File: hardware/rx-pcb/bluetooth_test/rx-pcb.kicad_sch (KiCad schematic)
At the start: 32 parts, among them J1 Conn_01x05_Pin, J2 Conn_01x04_Pin, J4 Conn_01x04_Pin, SW1 SW_SPST, U1 STM32WB05KZV6TR, U2 STS4L-AD1B-R3, U3 LMT70AYFQR, X1 Q22FA12800025, X2 ABS07-32.768KHZ-1-T

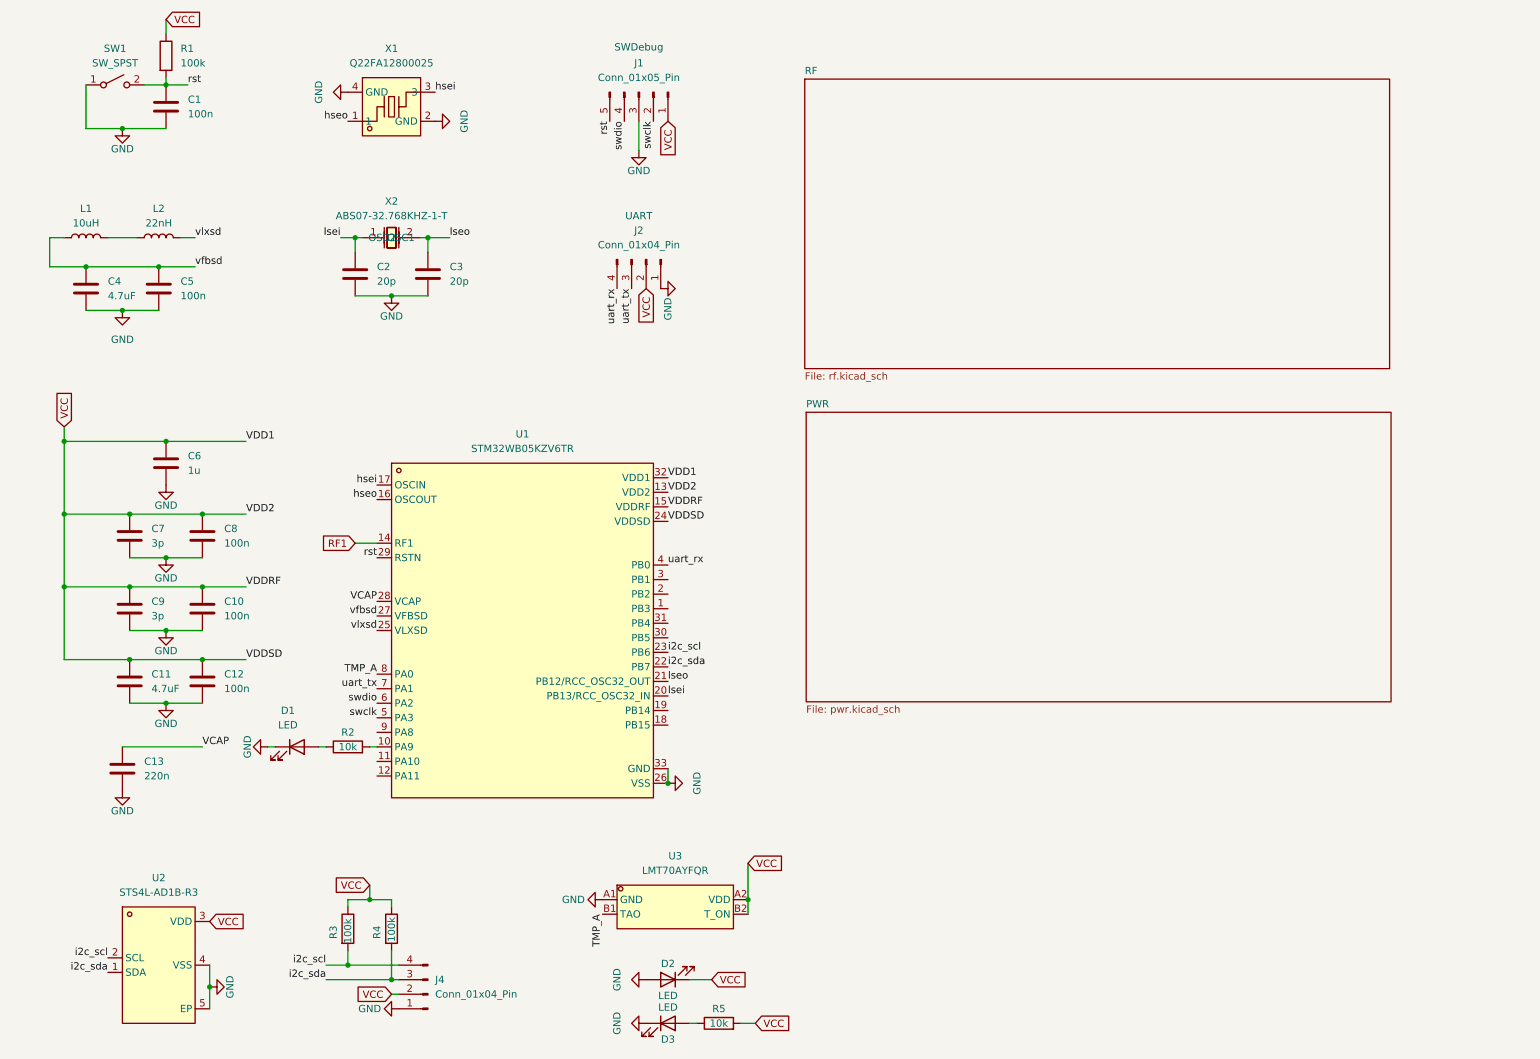
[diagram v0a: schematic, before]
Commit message: added selected diodes and bank capacitor. began board layout.
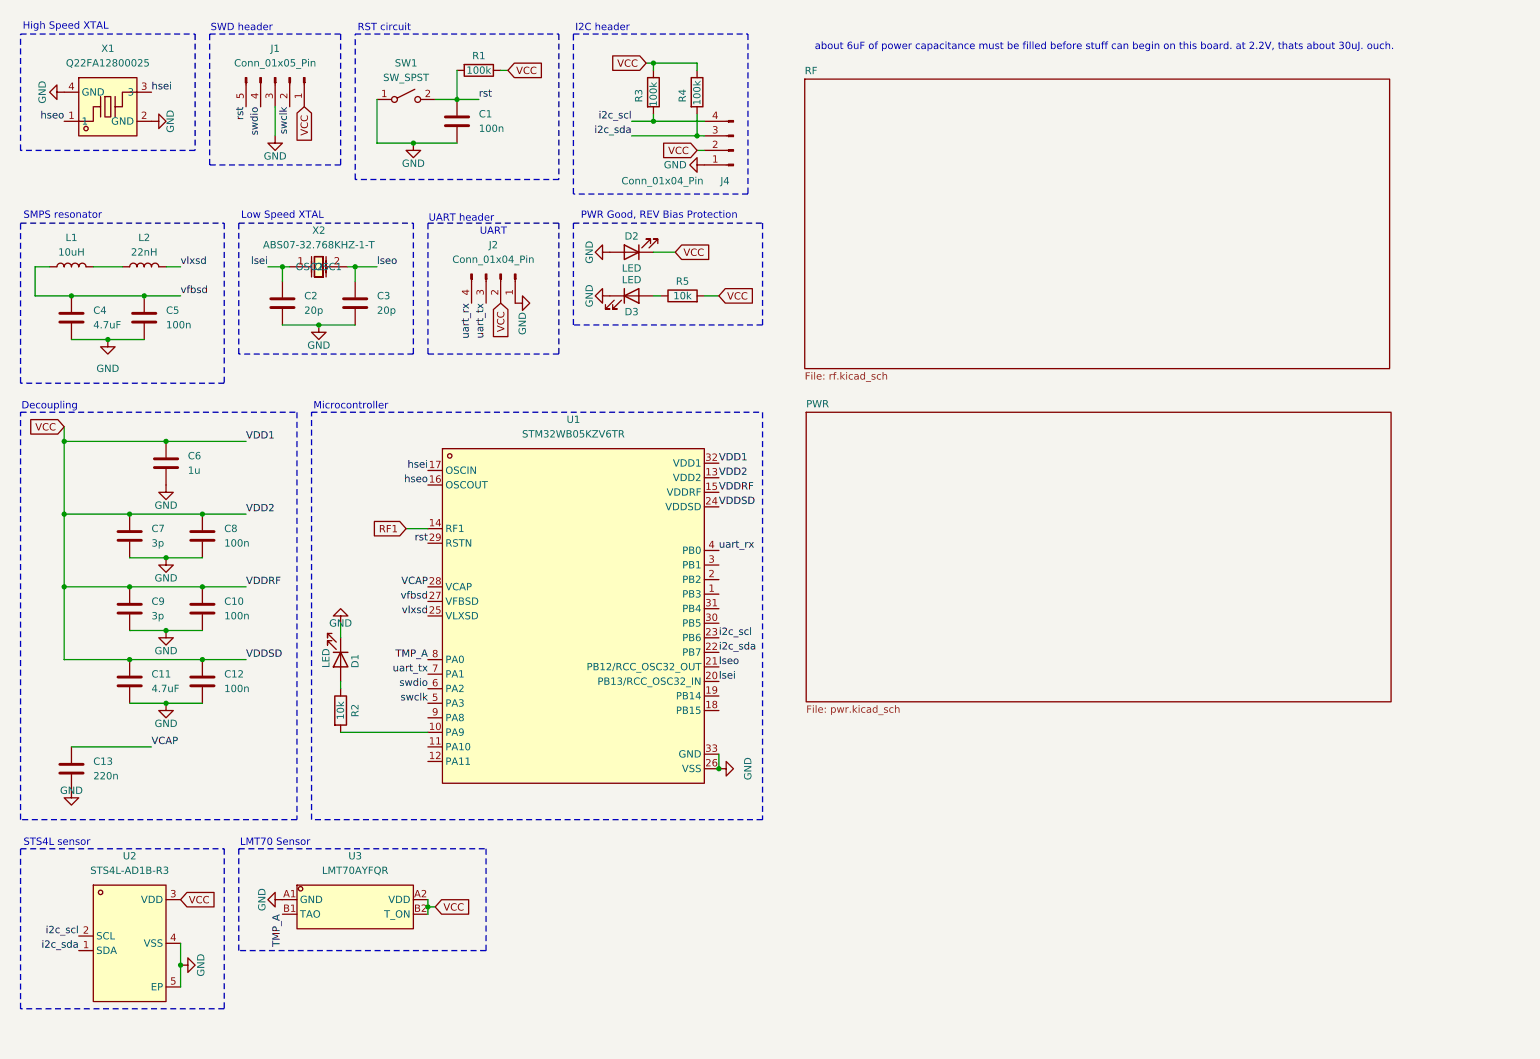
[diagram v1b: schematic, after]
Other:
- note added: "Decoupling"
- note added: "High Speed XTAL"
- note added: "I2C header"
- note added: "LMT70 Sensor"
- note added: "Low Speed XTAL"
- note added: "Microcontroller"
- note added: "PWR Good, REV Bias Protection"
- note added: "RST circuit"
- note added: "SMPS resonator"
- note added: "STS4L sensor"
- note added: "SWD header"
- note added: "UART header"
- note added: "about 6uF of power capacitance must be filled before stuff can begin on this board. at 2.2V, thats about 30uJ. ouch."
- note removed: "SWDebug"
- moved on the sheet: C1, C13, C2, C3, C4, C5, D1, D2, D3, J1, J2, J4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

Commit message: updated harvester with compartmentalization testing resistors and test points. updated bluetooth test to use a low Vf diode rather than an LED for reverse current protection. must update footprint for that.
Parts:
- removed D2: LED, rx-parts:LED_0805_2012Metric_Pad1.15x1.40mm_HandSolder, symbol rx-parts:LED
- removed R1: 100k, rx-parts:R_0805_2012Metric_Pad1.20x1.40mm_HandSolder, symbol rx-parts:R
- added D2: D, symbol Device:D
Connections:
- net GND: now also D2.2 (A)
- net VCC: now also D2.1 (K)
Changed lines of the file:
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@@
 	(rectangle
 		(start 111.76 17.78)
-		(end 142.24 45.72)
+		(end 144.78 45.72)
 		(stroke
 			(width 0)
@@
 	(wire
 		(pts
-			(xy 100.33 24.13) (xy 99.06 24.13)
-		)
-		(stroke
-			(width 0)
-			(type default)
-		)
-	)
-	(wire
-		(pts
 			(xy 34.29 114.3) (xy 46.99 114.3)
 		)
@@
 	(wire
 		(pts
-			(xy 91.44 24.13) (xy 91.44 29.21)
-		)
-		(stroke
-			(width 0)
-			(type default)
-		)
-	)
-	(wire
-		(pts
 			(xy 46.99 121.92) (xy 40.64 121.92)
 		)
@@
 	(global_label "VCC"
 		(shape input)
-		(at 100.33 24.13 0)
-		(fields_autoplaced yes)
-		(effects
-			(font
-				(size 1.27 1.27)
-			)
-			(justify left)
-		)
-		(property "Intersheetrefs" "${INTERSHEET_REFS}"
-			(at 106.9438 24.13 0)
-			(effects
-				(font
-					(size 1.27 1.27)
-				)
-				(justify left)
-				(hide yes)
-			)
-		)
-	)
-	(global_label "VCC"
-		(shape input)
 		(at 22.86 86.36 180)
 		(fields_autoplaced yes)
@@
 	)
 	(symbol
-		(lib_id "rx-parts:C")
-		(at 73.66 64.77 0)
+		(lib_id "Device:D")
+		(at 121.92 55.88 180)
 		(unit 1)
 		(exclude_from_sim no)
@@
 		(on_board yes)
 		(dnp no)
-		(fields_autoplaced yes)
-		(property "Reference" "C3"
-			(at 77.47 63.4999 0)
+		(property "Reference" "D2"
+			(at 122.174 53.34 0)
 			(effects
 				(font
 					(size 1.27 1.27)
 				)
-				(justify left)
 			)
 		)
-		(property "Value" "20p"
-			(at 77.47 66.0399 0)
+		(property "Value" "D"
+			(at 121.92 58.166 0)
 			(effects
 				(font
 					(size 1.27 1.27)
 				)
-				(justify left)
 			)
 		)
-		(property "Footprint" "rx-parts:C_0805_2012Metric_Pad1.18x1.45mm_HandSolder"
-			(at 74.6252 68.58 0)
+		(property "Footprint" ""
+			(at 121.92 55.88 0)
 			(effects
 				(font
@@
 		)
 		(property "Datasheet" "~"
-			(at 73.66 64.77 0)
+			(at 121.92 55.88 0)
 			(effects
 				(font
@@
 			)
 		)
-		(property "Description" "Unpolarized capacitor"
-			(at 73.66 64.77 0)
+		(property "Description" "Diode"
+			(at 121.92 55.88 0)
+			(effects
+				(font
+					(size 1.27 1.27)
+				)
+				(hide yes)
+			)
+		)
+		(property "Sim.Device" "D"
+			(at 121.92 55.88 0)
+			(effects
+				(font
+					(size 1.27 1.27)
+				)
+				(hide yes)
+			)
+		)
+		(property "Sim.Pins" "1=K 2=A"
+			(at 121.92 55.88 0)
 			(effects
 				(font
@@
 		)
 		(instances
-			(project "rx-pcb"
+			(project ""
 				(path "/9df8ddb8-545e-44cf-b4e7-941b19ec42ab"
-					(reference "C3")
+					(reference "D2")
 					(unit 1)
 				)
@@
 	)
 	(symbol
-		(lib_id "rx-parts:GND")
-		(at 40.64 96.52 0)
+		(lib_id "rx-parts:C")
+		(at 73.66 64.77 0)
 		(unit 1)
 		(exclude_from_sim no)
@@
 		(on_board yes)
 		(dnp no)
-		(property "Reference" "#PWR08"
-			(at 40.64 102.87 0)
+		(fields_autoplaced yes)
+		(property "Reference" "C3"
+			(at 77.47 63.4999 0)
 			(effects
 				(font
 					(size 1.27 1.27)
 				)
-				(hide yes)
+				(justify left)
 			)
 		)
-		(property "Value" "GND"
-			(at 40.64 100.076 0)
+		(property "Value" "20p"
+			(at 77.47 66.0399 0)
 			(effects
 				(font
 					(size 1.27 1.27)
 				)
+				(justify left)
 			)
 		)
-		(property "Footprint" ""
-			(at 40.64 96.52 0)
+		(property "Footprint" "rx-parts:C_0805_2012Metric_Pad1.18x1.45mm_HandSolder"
+			(at 74.6252 68.58 0)
 			(effects
 				(font
@@
 			)
 		)
-		(property "Datasheet" ""
-			(at 40.64 96.52 0)
+		(property "Datasheet" "~"
+			(at 73.66 64.77 0)
 			(effects
 				(font
@@
 			)
 		)
-		(property "Description" "Power symbol creates a global label with name \"GND\" , ground"
-			(at 40.64 96.52 0)
+		(property "Description" "Unpolarized capacitor"
+			(at 73.66 64.77 0)
 			(effects
 				(font
@@
 			)
 		)
+		(pin "2"
+		)
 		(pin "1"
 		)
@@
 			(project "rx-pcb"
 				(path "/9df8ddb8-545e-44cf-b4e7-941b19ec42ab"
-					(reference "#PWR08")
+					(reference "C3")
 					(unit 1)
 				)
@@
 	(symbol
 		(lib_id "rx-parts:GND")
-		(at 134.62 40.64 270)
+		(at 40.64 96.52 0)
 		(unit 1)
 		(exclude_from_sim no)
@@
 		(on_board yes)
 		(dnp no)
-		(property "Reference" "#PWR019"
-			(at 128.27 40.64 0)
+		(property "Reference" "#PWR08"
+			(at 40.64 102.87 0)
 			(effects
 				(font
@@
 		)
 		(property "Value" "GND"
-			(at 129.54 40.64 90)
+			(at 40.64 100.076 0)
 			(effects
 				(font
@@
 		)
 		(property "Footprint" ""
-			(at 134.62 40.64 0)
+			(at 40.64 96.52 0)
 			(effects
 				(font
@@
 		)
 		(property "Datasheet" ""
-			(at 134.62 40.64 0)
+			(at 40.64 96.52 0)
 			(effects
 				(font
@@
 		)
 		(property "Description" "Power symbol creates a global label with name \"GND\" , ground"
-			(at 134.62 40.64 0)
+			(at 40.64 96.52 0)
 			(effects
 				(font
@@
 			(project "rx-pcb"
 				(path "/9df8ddb8-545e-44cf-b4e7-941b19ec42ab"
-					(reference "#PWR019")
+					(reference "#PWR08")
 					(unit 1)
 				)
@@
 	)
 	(symbol
-		(lib_id "rx-parts:LED")
-		(at 121.92 55.88 180)
+		(lib_id "rx-parts:GND")
+		(at 134.62 40.64 270)
 		(unit 1)
 		(exclude_from_sim no)
@@
 		(on_board yes)
 		(dnp no)
-		(property "Reference" "D2"
-			(at 121.92 53.086 0)
-			(effects
-				(font
-					(size 1.27 1.27)
-				)
-			)
-		)
-		(property "Value" "LED"
-			(at 121.92 58.674 0)
+		(property "Reference" "#PWR019"
+			(at 128.27 40.64 0)
 			(effects
 				(font
 					(size 1.27 1.27)
 				)
+				(hide yes)
 			)
 		)
-		(property "Footprint" "rx-parts:LED_0805_2012Metric_Pad1.15x1.40mm_HandSolder"
-			(at 121.92 55.88 0)
+		(property "Value" "GND"
+			(at 129.54 40.64 90)
 			(effects
 				(font
 					(size 1.27 1.27)
 				)
-				(hide yes)
 			)
 		)
-		(property "Datasheet" "~"
-			(at 121.92 55.88 0)
+		(property "Footprint" ""
+			(at 134.62 40.64 0)
 			(effects
 				(font
@@
 			)
 		)
-		(property "Description" "Light emitting diode"
-			(at 121.92 55.88 0)
+		(property "Datasheet" ""
+			(at 134.62 40.64 0)
 			(effects
 				(font
@@
 			)
 		)
-		(property "Sim.Pins" "1=K 2=A"
-			(at 121.92 55.88 0)
+		(property "Description" "Power symbol creates a global label with name \"GND\" , ground"
+			(at 134.62 40.64 0)
 			(effects
 				(font
@@
 			)
 		)
-		(pin "2"
-		)
 		(pin "1"
 		)
 		(instances
-			(project ""
+			(project "rx-pcb"
 				(path "/9df8ddb8-545e-44cf-b4e7-941b19ec42ab"
-					(reference "D2")
+					(reference "#PWR019")
 					(unit 1)
 				)
@@
 					(unit 1)
 				)
-			)
-		)
-	)
-	(symbol
-		(lib_id "rx-parts:R")
-		(at 95.25 24.13 270)
-		(unit 1)
-		(exclude_from_sim no)
-		(in_bom yes)
-		(on_board yes)
-		(dnp no)
-		(property "Reference" "R1"
-			(at 95.25 21.59 90)
-			(effects
-				(font
-					(size 1.27 1.27)
-				)
-			)
-		)
-		(property "Value" "100k"
-			(at 95.25 24.13 90)
-			(effects
-				(font
-					(size 1.27 1.27)
-				)
-			)
-		)
-		(property "Footprint" "rx-parts:R_0805_2012Metric_Pad1.20x1.40mm_HandSolder"
-			(at 95.25 22.352 90)
-			(effects
-				(font
-					(size 1.27 1.27)
-				)
-				(hide yes)
-			)
-		)
-		(property "Datasheet" "~"
-			(at 95.25 24.13 0)
-			(effects
-				(font
-					(size 1.27 1.27)
-				)
-				(hide yes)
-			)
-		)
-		(property "Description" "Resistor"
-			(at 95.25 24.13 0)
-			(effects
-				(font
-					(size 1.27 1.27)
-				)
-				(hide yes)
-			)
-		)
-		(pin "2"
-		)
-		(pin "1"
-		)
-		(instances
-			(project ""
-				(path "/9df8ddb8-545e-44cf-b4e7-941b19ec42ab"
-					(reference "R1")
-					(unit 1)
-				)

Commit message: fixed merge errors, re updated rx-pcb
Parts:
- removed D2: D, symbol Device:D
- added C14: 20p, Capacitor_SMD:C_0201_0603Metric_Pad0.64x0.40mm_HandSolder, symbol Device:C
- added FL1: MLPF-WB-01D3, rx-parts:BGA-6_L1.6-W1.0-R3-C2-P0.50-TL, symbol rx-parts:MLPF-WB-01D3
- added J3: Conn_Coaxial_Small, rx-parts:SMA_Amphenol_901-143_Horizontal, symbol rx-parts:Conn_Coaxial_Small
- added J5: Conn_01x02_Pin, Connector_PinHeader_2.54mm:PinHeader_1x02_P2.54mm_Vertical, symbol Connector:Conn_01x02_Pin
- U2: footprint easyeda2kicad:DFN-4_L1.5-W1.5-P0.80-TL-EP -> rx-parts:DFN-4_L1.5-W1.5-P0.80-TL-EP
- U3: footprint easyeda2kicad:DSBGA-4_L0.8-W0.8-R2-C2-P0.40-BL -> rx-parts:DSBGA-4_L0.8-W0.8-R2-C2-P0.40-BL
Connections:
- net GND: now also FL1.A2 (GND4), FL1.B1 (GND3), FL1.B2 (GND2), FL1.B3 (GND1), J3.2 (Ext), J5.2 (Pin_2)
- net RF1: now also C14.1
- net TMP_A: now also U1.1 (PB3); no longer U1.8 (PA0)
- net VCC: now also J5.1 (Pin_1)
- new net: C14.2, FL1.A3 (IN)
- new net ANT: FL1.A1 (OUT), J3.1 (In)
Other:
- removed sheet PWR
- removed sheet RF
- note added: "40 OHM"
- note added: "50 OHM"
- note added: "PWR Good"
- note removed: "PWR Good, REV Bias Protection"
- moved on the sheet: D3, R5

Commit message: backup of sensor-bluetooth board. re-wiring it.
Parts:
- added D2: D_Zener, Diode_SMD:D_0603_1608Metric_Pad1.05x0.95mm_HandSolder, symbol Device:D_Zener
- added J6: Conn_01x02_Pin, Connector_PinHeader_2.54mm:PinHeader_1x02_P2.54mm_Vertical, symbol Connector:Conn_01x02_Pin
- added R1, R10, R6, R7, R8, R9: 0, Resistor_SMD:R_0201_0603Metric_Pad0.64x0.40mm_HandSolder, symbol rx-parts:R
- C1, C10, C11, C12, C13, C2, C3, C4, C5, C6, C7, C8, C9: footprint rx-parts:C_0805_2012Metric_Pad1.18x1.45mm_HandSolder -> Capacitor_SMD:C_0603_1608Metric_Pad1.08x0.95mm_HandSolder
- R3, R4: value 100k -> 50k
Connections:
- net GND: now also D2.2 (A), J6.1 (Pin_1)
- net VCC: now also D2.1 (K)
- net i2c_scl: now also R1.2; no longer U1.23 (PB6)
- net i2c_sda: now also R6.1; no longer U1.22 (PB7)
- net swclk: now also R9.2; no longer U1.5 (PA3)
- net swdio: now also R8.2; no longer U1.6 (PA2)
- net uart_rx: now also R10.1; no longer U1.4 (PB0)
- net uart_tx: now also R7.1; no longer U1.7 (PA1)
- net ADC_jump: now reaches U1.3 (PB1)
- net ADC_jump: now also J6.2 (Pin_2)
- new net: R9.1, U1.5 (PA3)
- new net: R8.1, U1.6 (PA2)
- new net: R7.2, U1.7 (PA1)
- new net: R10.2, U1.4 (PB0)
- new net: R1.1, U1.23 (PB6)
- new net: R6.2, U1.22 (PB7)
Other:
- moved on the sheet: C14, D1, FL1, J3, J5, R2

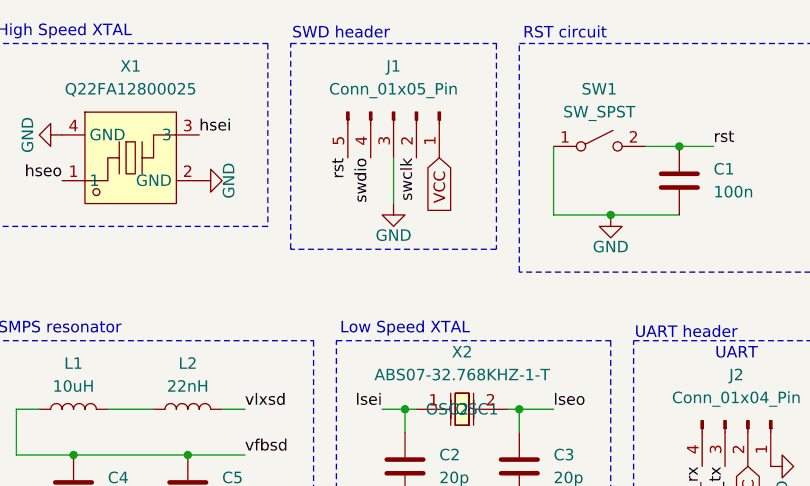
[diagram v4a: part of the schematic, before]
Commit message: updated rx-board with compartmentalization resistors, updated silkscreen
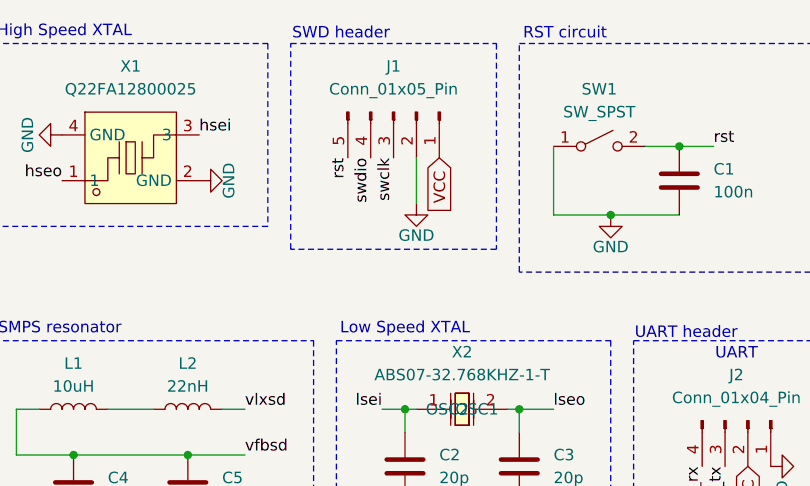
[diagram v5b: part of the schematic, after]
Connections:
- net GND: now also J1.2 (Pin_2); no longer J1.3 (Pin_3)
- net swclk: now also J1.3 (Pin_3); no longer J1.2 (Pin_2)
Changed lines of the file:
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@@
 	(wire
 		(pts
-			(xy 59.69 35.56) (xy 59.69 30.48)
+			(xy 62.23 35.56) (xy 62.23 30.48)
 		)
 		(stroke
@@
 	)
 	(label "swclk"
-		(at 62.23 30.48 270)
+		(at 59.69 30.48 270)
 		(effects
 			(font
@@
 	(symbol
 		(lib_id "rx-parts:GND")
-		(at 59.69 35.56 0)
+		(at 62.23 35.56 0)
 		(unit 1)
 		(body_style 1)
@@
 		(dnp no)
 		(property "Reference" "#PWR04"
-			(at 59.69 41.91 0)
+			(at 62.23 41.91 0)
 			(hide yes)
 			(show_name no)
@@
 		)
 		(property "Value" "GND"
-			(at 59.69 39.116 0)
+			(at 62.23 39.116 0)
 			(show_name no)
 			(do_not_autoplace no)
@@
 		)
 		(property "Footprint" ""
-			(at 59.69 35.56 0)
+			(at 62.23 35.56 0)
 			(hide yes)
 			(show_name no)
@@
 		)
 		(property "Datasheet" ""
-			(at 59.69 35.56 0)
+			(at 62.23 35.56 0)
 			(hide yes)
 			(show_name no)
@@
 		)
 		(property "Description" "Power symbol creates a global label with name \"GND\" , ground"
-			(at 59.69 35.56 0)
-			(hide yes)
-			(show_name no)
+			(at 62.23 35.56 0)
+			(hide yes)
+			(show_name no)

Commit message: updates for dr weeks
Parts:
- removed D3: LED, rx-parts:LED_0805_2012Metric_Pad1.15x1.40mm_HandSolder, symbol rx-parts:LED
- removed J6: Conn_01x02_Pin, Connector_PinHeader_2.54mm:PinHeader_1x02_P2.54mm_Vertical, symbol Connector:Conn_01x02_Pin
- removed R5: 10k, rx-parts:R_0805_2012Metric_Pad1.20x1.40mm_HandSolder, symbol rx-parts:R
- removed U3: LMT70AYFQR, rx-parts:DSBGA-4_L0.8-W0.8-R2-C2-P0.40-BL, symbol easyeda2kicad:LMT70AYFQR
- added U3: STS4L-AD1B-R3, rx-parts:DFN-4_L1.5-W1.5-P0.80-TL-EP, symbol easyeda2kicad:STS4L-AD1B-R3
- C1, C10, C11, C12, C13, C2, C3, C4, C5, C6, C7, C8, C9: footprint Capacitor_SMD:C_0603_1608Metric_Pad1.08x0.95mm_HandSolder -> Capacitor_SMD:C_0805_2012Metric_Pad1.18x1.45mm_HandSolder
- J3: footprint rx-parts:SMA_Amphenol_901-143_Horizontal -> Connector_Coaxial:SMA_Samtec_SMA-J-P-H-ST-EM1_EdgeMount
- R1, R6: footprint Resistor_SMD:R_0201_0603Metric_Pad0.64x0.40mm_HandSolder -> Resistor_SMD:R_0805_2012Metric_Pad1.20x1.40mm_HandSolder
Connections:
- net GND: now also U3.4 (VSS), U3.5 (EP)
- net VCC: now also U3.3 (VDD)
- net i2c_scl: now also U3.2 (SCL)
- net i2c_sda: now also U3.1 (SDA)
- net ADC_jump: no longer names the net of U1.3 (PB1)
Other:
- note removed: "PWR Good"
